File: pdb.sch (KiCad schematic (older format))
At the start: 0 parts

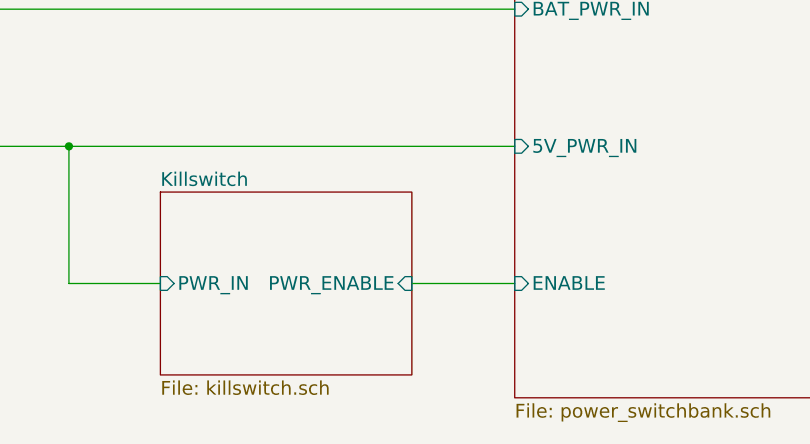
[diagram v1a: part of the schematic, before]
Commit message: add high power switch
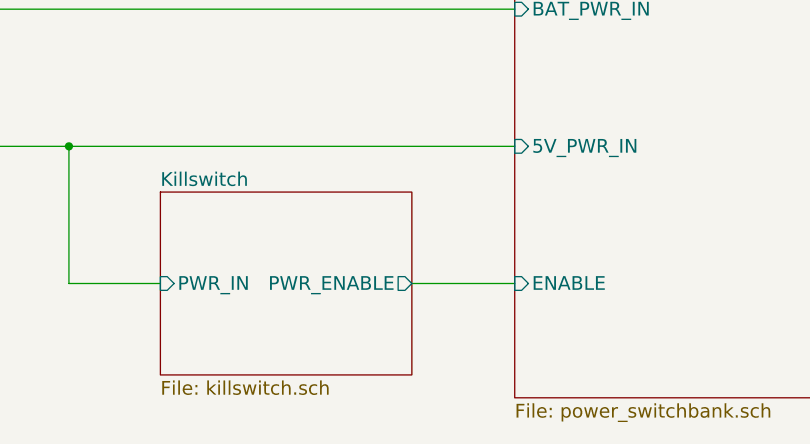
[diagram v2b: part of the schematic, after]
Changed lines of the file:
@@
 LIBS:valves
 LIBS:ltc1473
-LIBS:agg-kicad
 LIBS:nmos_sssgd
 LIBS:ehhd015a0a
@@
 LIBS:tps2024d
 LIBS:its5215l
+LIBS:agg-kicad
 LIBS:pdb-cache
 EELAYER 25 0
@@
 $Descr A4 11693 8268
 encoding utf-8
-Sheet 1 7
+Sheet 1 8
 Title "Power Distribution Board"
 Date "2017-07-02"
@@
 F1 "killswitch.sch" 60
 F2 "PWR_IN" I L 6750 4400 60
-F3 "PWR_ENABLE" I R 7850 4400 60
+F3 "PWR_ENABLE" O R 7850 4400 60
 $EndSheet
 Wire Wire Line

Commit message: power switches connect to pgnd
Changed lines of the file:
@@
 Wire Wire Line
 	1650 3400 2250 3400
+$Comp
+L GND #PWR?
+U 1 1 5962BA8D
+P 2350 5900
+F 0 "#PWR?" H 2350 5650 50  0001 C CNN
+F 1 "GND" H 2350 5750 50  0000 C CNN
+F 2 "" H 2350 5900 50  0001 C CNN
+F 3 "" H 2350 5900 50  0001 C CNN
+	1    2350 5900
+	1    0    0    -1
+$EndComp
+$Comp
+L PGND #PWR?
+U 1 1 5962BADD
+P 2600 5950
+F 0 "#PWR?" H 2470 5990 50  0001 L CNN
+F 1 "PGND" H 2600 5850 50  0000 C CNN
+F 2 "" H 2600 5950 60  0001 C CNN
+F 3 "" H 2600 5950 60  0001 C CNN
+	1    2600 5950
+	1    0    0    -1
+$EndComp
+Wire Wire Line
+	2350 5900 2350 5800
+Wire Wire Line
+	2350 5800 2600 5800
+Wire Wire Line
+	2600 5800 2600 5950
 $EndSCHEMATC
